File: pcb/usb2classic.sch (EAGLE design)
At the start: 28 parts, among them IC2 74HC595N, IC3 74HC595N, IC6 EPM7064S44, IC7 74HC153N, IC8 74HC153N, X2 GLX-S-88M, X5 2510-, X6 GLX-S-88M

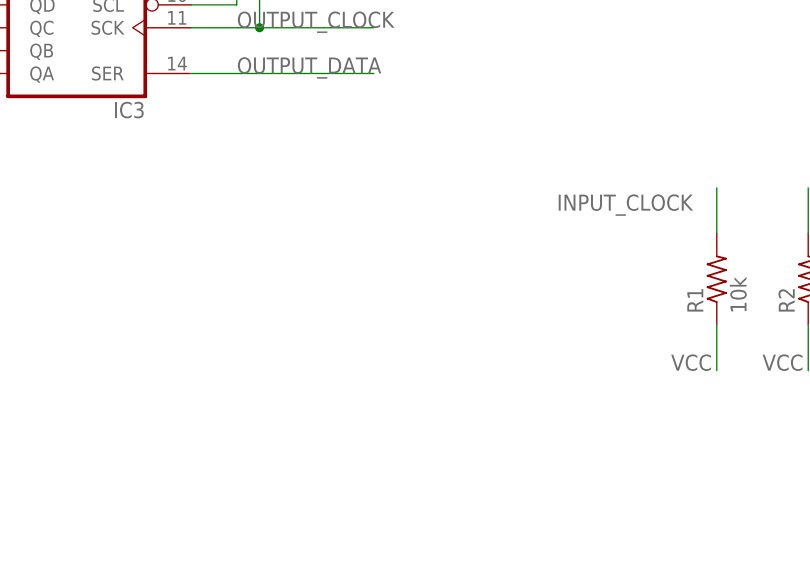
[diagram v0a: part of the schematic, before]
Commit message: Added pull-down resistor to NES/SNES data line. This is an attempt to fix issue #1
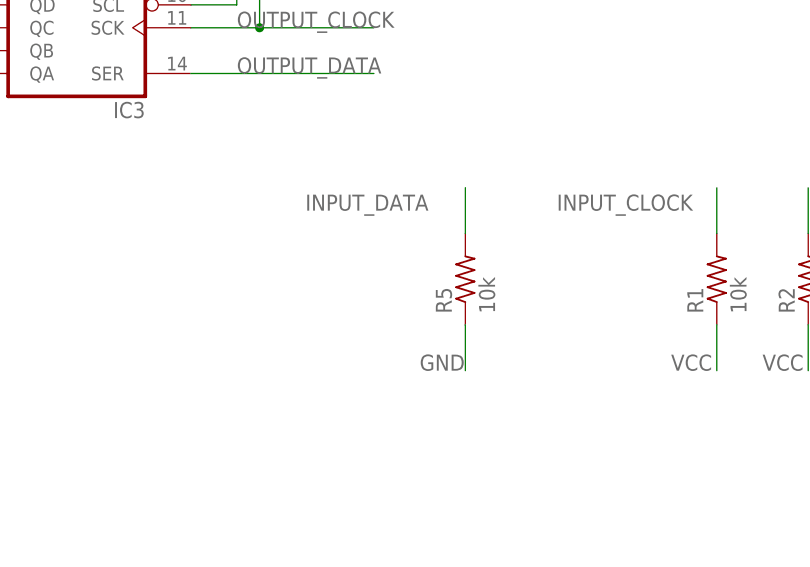
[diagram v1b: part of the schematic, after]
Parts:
- added R5: 10k, resistor:R-US_0207/10
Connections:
- net GND: now also R5.1
- net INPUT_DATA: now also R5.2
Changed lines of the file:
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@@
 <part name="JP1" library="pinhead" deviceset="PINHD-1X10" device=""/>
 <part name="JP2" library="pinhead" deviceset="PINHD-1X10" device=""/>
+<part name="R5" library="resistor" deviceset="R-US_" device="0207/10" value="10k"/>
 </parts>
 <sheets>
@@
 <instance part="JP1" gate="A" x="271.78" y="-88.9"/>
 <instance part="JP2" gate="A" x="292.1" y="-88.9"/>
+<instance part="R5" gate="G$1" x="157.48" y="-27.94" rot="R90"/>
 </instances>
 <busses>
@@
 <label x="259.08" y="-93.98" size="1.778" layer="95"/>
 </segment>
+<segment>
+<pinref part="R5" gate="G$1" pin="1"/>
+<wire x1="157.48" y1="-33.02" x2="157.48" y2="-38.1" width="0.1524" layer="91"/>
+<label x="152.4" y="-38.1" size="1.778" layer="95"/>
+</segment>
 </net>
 <net name="OUTPUT_DATA" class="0">
@@
 <label x="383.54" y="17.78" size="1.778" layer="95"/>
 </segment>
-</net>
+<segment>
+<pinref part="R5" gate="G$1" pin="2"/>
+<wire x1="157.48" y1="-22.86" x2="157.48" y2="-17.78" width="0.1524" layer="91"/>
+<label x="139.7" y="-20.32" size="1.778" layer="95"/>
+</segment>
+</net>

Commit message: Removed not used signal traces from the CPLD
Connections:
- net O12: no longer IC60.IO3
- net O13: no longer IC60.IO51
- net O14: no longer IC60.IO19
- net O15: no longer IC60.OE1
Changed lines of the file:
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@@
-</segment>
-<segment>
-<pinref part="IC6" gate="0" pin="IO3"/>
-<wire x1="398.78" y1="60.96" x2="383.54" y2="60.96" width="0.1524" layer="91"/>
-<label x="383.54" y="60.96" size="1.778" layer="95"/>
 </segment>
 <segment>
@@
 </segment>
 <segment>
-<pinref part="IC6" gate="0" pin="IO51"/>
-<wire x1="398.78" y1="0" x2="383.54" y2="0" width="0.1524" layer="91"/>
-<label x="383.54" y="0" size="1.778" layer="95"/>
-</segment>
-<segment>
 <pinref part="RN2" gate="1" pin="7"/>
 <wire x1="228.6" y1="33.02" x2="228.6" y2="38.1" width="0.1524" layer="91"/>
@@
 <label x="91.44" y="45.72" size="1.778" layer="95"/>
 <pinref part="IC2" gate="A" pin="QG"/>
-</segment>
-<segment>
-<pinref part="IC6" gate="0" pin="IO19"/>
-<wire x1="398.78" y1="40.64" x2="383.54" y2="40.64" width="0.1524" layer="91"/>
-<label x="383.54" y="40.64" size="1.778" layer="95"/>
 </segment>
 <segment>
@@
 </segment>
 <segment>
-<pinref part="IC6" gate="0" pin="OE1"/>
-<wire x1="398.78" y1="71.12" x2="381" y2="71.12" width="0.1524" layer="91"/>
-<label x="381" y="71.12" size="1.778" layer="95"/>
-</segment>
-<segment>
